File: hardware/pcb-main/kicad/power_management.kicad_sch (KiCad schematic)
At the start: 56 parts, among them J7 TYPE-C-31-M-12, J8 JST_PH_2pin, Q2 PMOS, SW1 SS-12D10L5, U5 BQ24195RGER, U6 TPS61088RHLR, U7 INA219AIDCNR, U8 AMS1117-3.3, U9 USBLC6-2SC6

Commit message: Complete Phase 1d/1e: manual wiring, ERC clean (0 errors)
Root sheet:
- Wire ESP32_S3 sheet pins to system nets via labels (I2C_SDA,
  I2C_SCL, TCA_RESET, LED_DATA, CHRG_INT, USB_DP, USB_DN)
- Connect power pins with +3.3V, +5V, GND power symbols
- Add PWR_FLAG symbols to resolve power-not-driven ERC errors
- NC flags on INT1/2/3 (design decision to drop interrupt lines)
- Remove TPIO11/12/13 (INT test points, no longer needed)
- Clean up dangling wires from old U2/U1 area
- Remove stray I2C_SCL hierarchical label

Power management sheet:
- Wire J7 D+/D- pads (A6/B6 tied to USB_DP, A7/B7 tied to USB_DN)
- Insert VSYS_SW into power path: R44 and INA219 IN+ now on
  VSYS_SW net so SW1 actually disconnects boost converter input
- Position AMS1117, caps, USBLC6, power switch components

ESP32_S3 sheet:
- Add no-connect on D5 DOUT (status LED has no downstream chain)
- Component positioning cleanup

ERC: 0 errors, 69 warnings (all benign JLC-MCP pin type mismatches
and footprint library path issues)

Made-with: Cursor
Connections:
- net USB_DN: now also J7.A7 (DN1), J7.B7 (DN2)
- net USB_DP: now also J7.A6 (DP1), J7.B6 (DP2)
- net VSYS: no longer R44.1, U7.1 (IN+)
- net VSYS_SW: now also R44.1, U7.1 (IN+)
- no-connect marks 9 -> 5
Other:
- moved on the sheet: C20, C21, C22, C23, C24, C25, C26, C27, C28, C29, C30, C31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

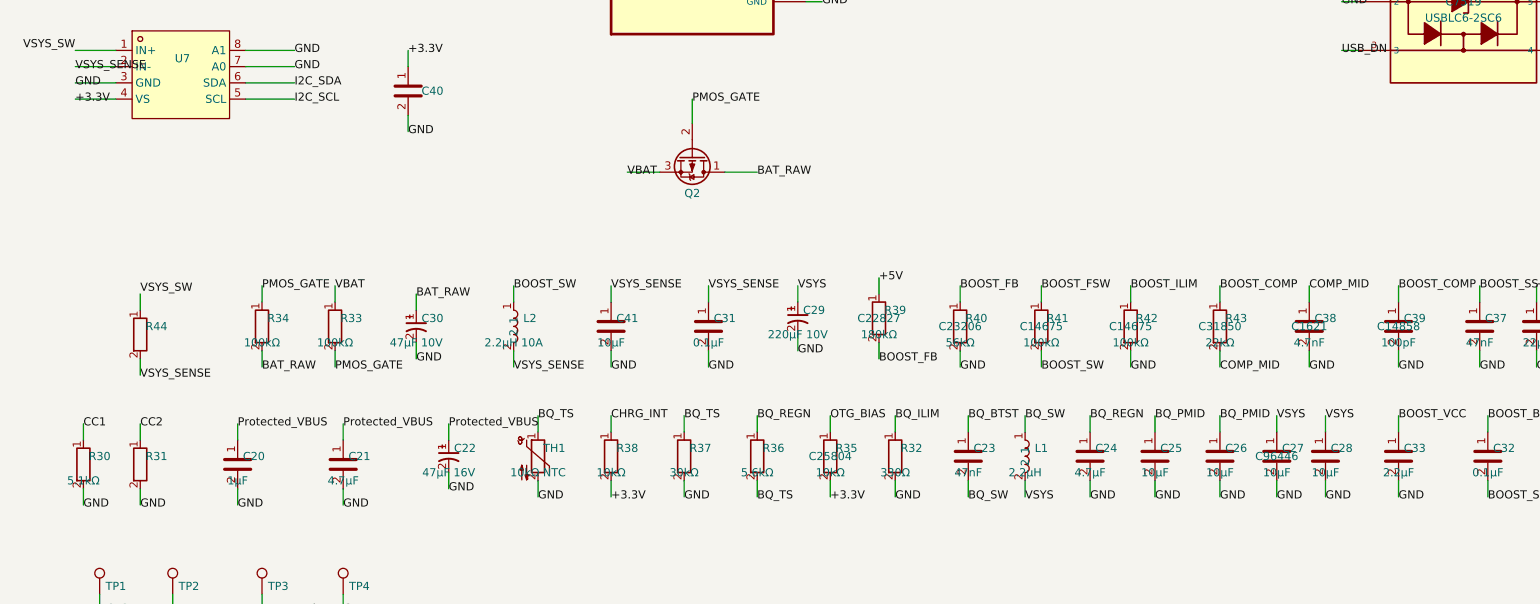
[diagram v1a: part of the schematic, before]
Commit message: Fixed polarity protection on the power circuit
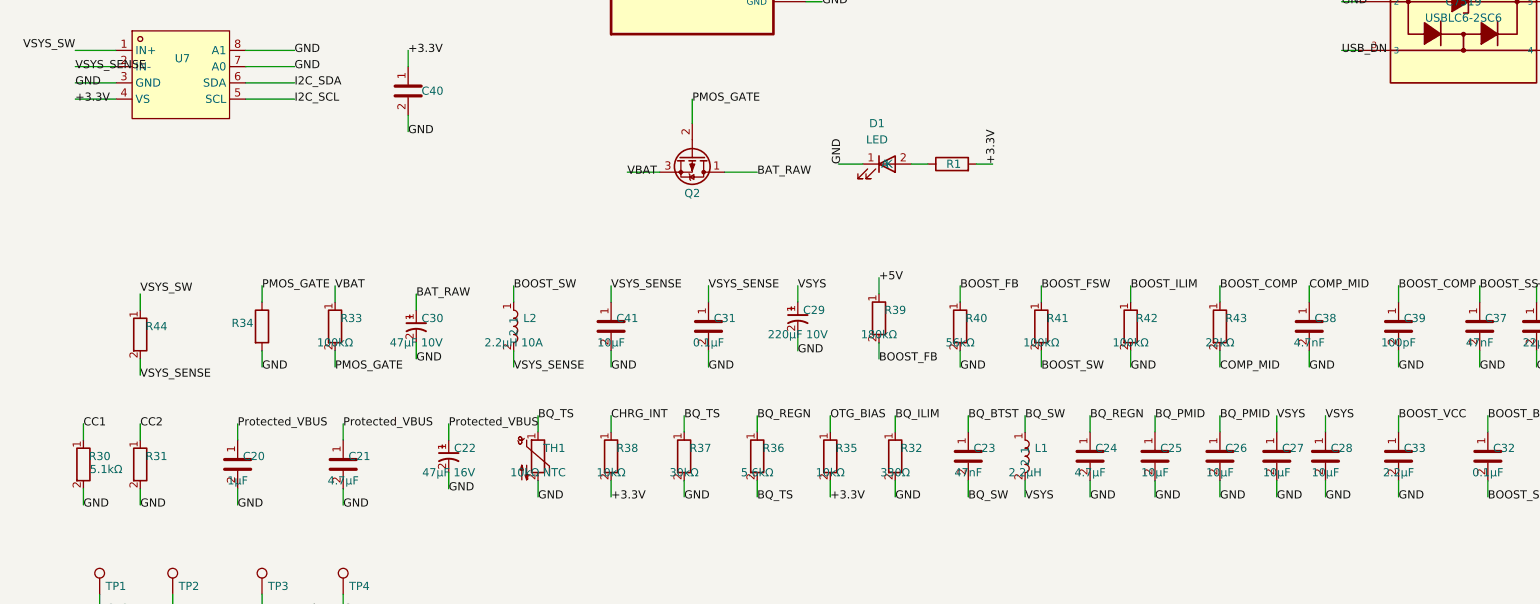
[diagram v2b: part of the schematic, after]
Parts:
- added D1: LED, LED_SMD:LED_0603_1608Metric, symbol Device:LED
- added R1: 1kΩ, Resistor_SMD:R_0603_1608Metric, symbol Device:R
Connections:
- net +3.3V: now also R1.2
- net BAT_RAW: no longer R34.2
- net GND: now also R34.2, D1.1 (K)
- new net: D1.2 (A), R1.1
